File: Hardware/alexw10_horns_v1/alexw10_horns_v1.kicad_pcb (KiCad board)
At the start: 2 copper layers, 50 x 34 mm, 28 parts, among them J1 Conn_01x03, J2 Conn_01x02, J3 Conn_01x02, J4 Conn_01x02, Q1 Q_NMOS_DGS, SW1 SW_Push_SPDT

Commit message: finished horns
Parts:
- C8: footprint Capacitor_SMD:CP_Elec_8x5.4 -> Capacitor_SMD:CP_Elec_6.3x7.7
- D1: footprint Diode_SMD:D_1812_4532Metric -> Diode_SMD:D_1206_3216Metric
- moved D1 0.86 mm to (131.5, 81.0)
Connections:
- SW1 pad 1: /V_divider3.3V -> /HORN_CTL
- SW1 pad 3: /HORN_CTL -> /V_divider3.3V
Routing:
- net /V_divider3.3V: track 15.0 -> 18.3 mm, vias 0 -> 2
- net /HORN_CTL: track 14.0 -> 16.3 mm
- net /HORN_IN: track 21.9 -> 22.6 mm

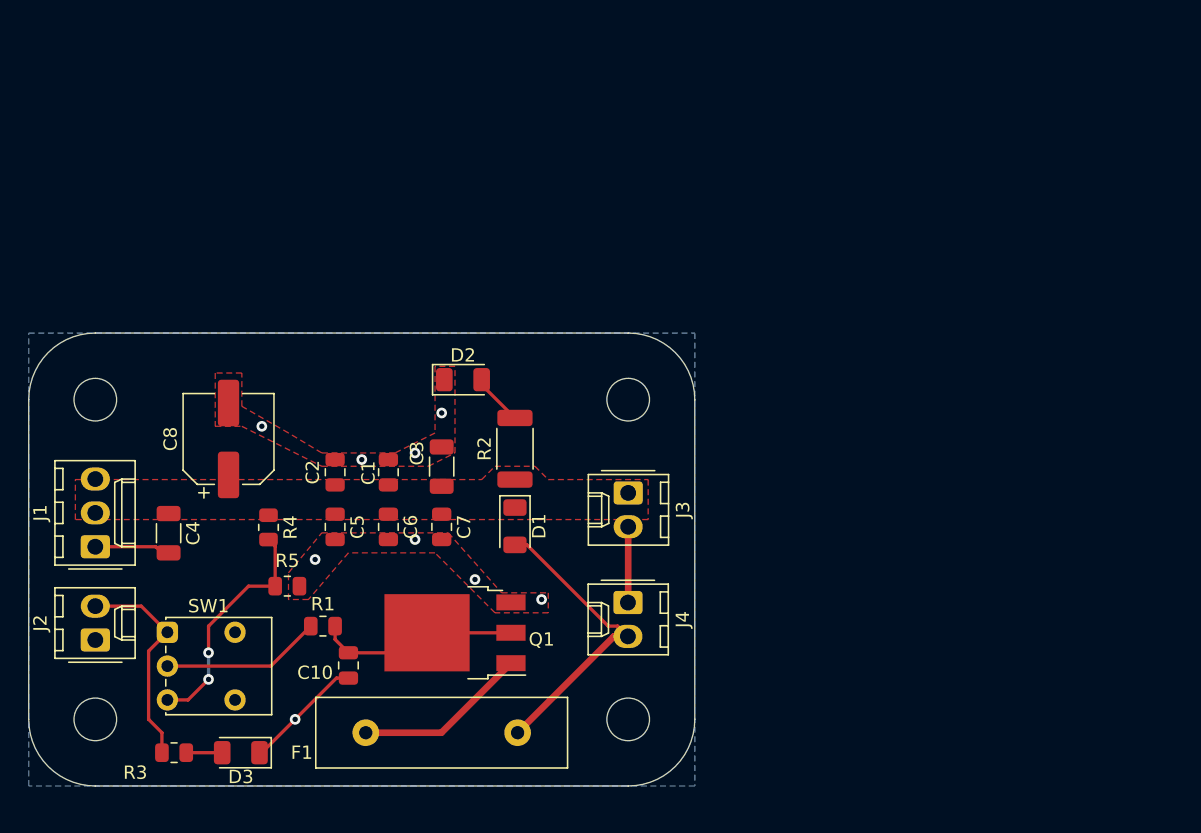
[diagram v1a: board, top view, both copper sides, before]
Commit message: fixed things related to horns such as changing connectors, removing the switch, and removing power planes as well as general rerouting of everything
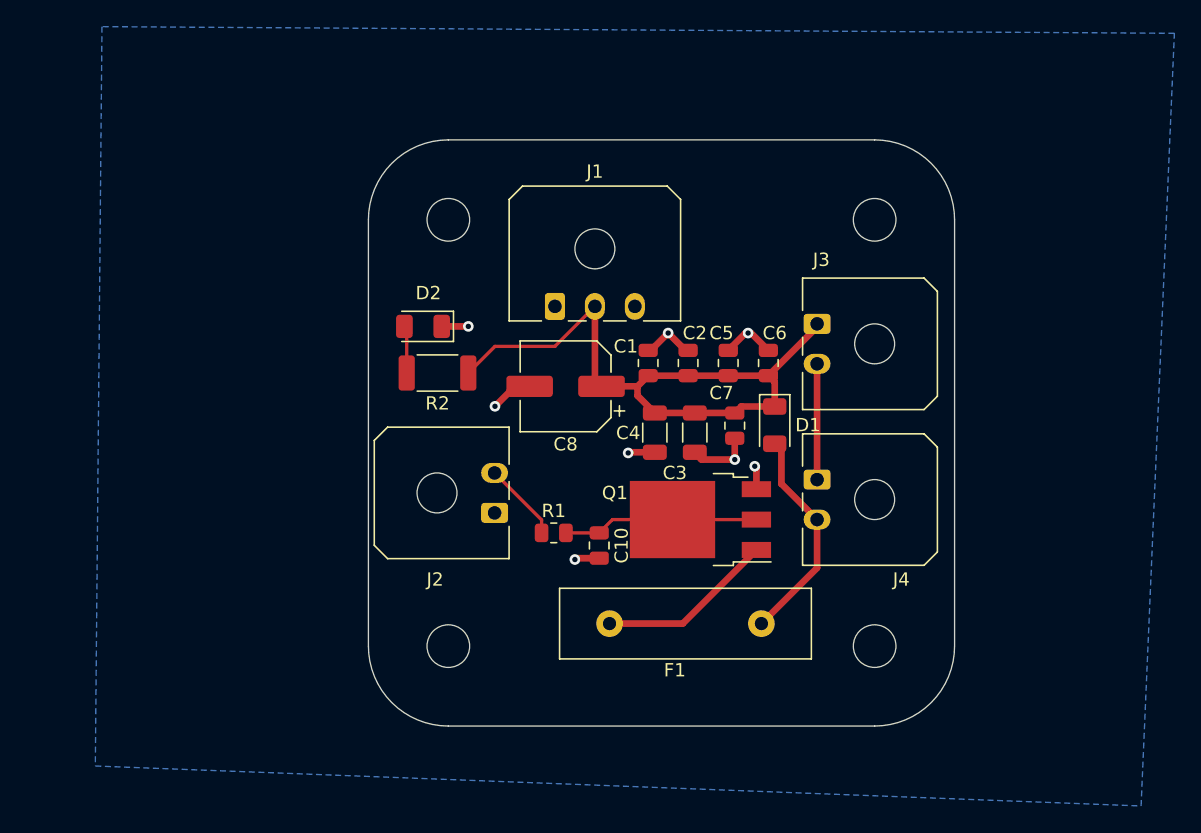
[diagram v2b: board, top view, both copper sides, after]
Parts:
- removed D3: GREEN_LED, LED_SMD:LED_1206_3216Metric
- removed R3: 130, Resistor_SMD:R_0805_2012Metric
- removed R4: 15k, Resistor_SMD:R_0805_2012Metric
- removed R5: 2.4k, Resistor_SMD:R_0805_2012Metric
- removed the REF** at (100.0, 71.5)
- removed the REF** at (100.0, 95.5)
- removed the REF** at (140.0, 71.5)
- removed the REF** at (140.0, 95.5)
- removed SW1: SW_Push_SPDT, Button_Switch_THT:SW_Push_1P2T_Vertical_E-Switch_800UDP8P1A1M6
- added REF**: MountingHole_3.2mm_M3, MountingHole:MountingHole_3.2mm_M3, F.Cu at (158.5, 58.0)
- added REF**: MountingHole_3.2mm_M3, MountingHole:MountingHole_3.2mm_M3, F.Cu at (158.5, 90.0)
- added REF**: MountingHole_3.2mm_M3, MountingHole:MountingHole_3.2mm_M3, F.Cu at (126.5, 58.0)
- added REF**: MountingHole_3.2mm_M3, MountingHole:MountingHole_3.2mm_M3, F.Cu at (126.5, 90.0)
- J1: footprint Connector_Molex:Molex_KK-254_AE-6410-03A_1x03_P2.54mm_Vertical -> Connector_Molex:Molex_Micro-Fit_3.0_43650-0300_1x03_P3.00mm_Horizontal
- J2, J3, J4: footprint Connector_Molex:Molex_KK-254_AE-6410-02A_1x02_P2.54mm_Vertical -> Connector_Molex:Molex_Micro-Fit_3.0_43650-0200_1x02_P3.00mm_Horizontal
- moved J1 38.9 mm to (134.5, 64.5), turned to 0 degrees
- moved C4 37.3 mm to (142.0, 74.0)
- moved C5 32.0 mm to (147.5, 68.8), turned to 90 degrees
- moved J2 31.5 mm to (130.0, 80.0)
- moved C6 31.1 mm to (150.5, 68.8), turned to 90 degrees
- moved C2 27.7 mm to (144.5, 68.8)
- moved C8 25.6 mm to (135.3, 70.5), turned to 180 degrees
- moved C7 23.3 mm to (148.0, 73.5)
- moved C1 21.2 mm to (141.5, 68.8)
- moved D1 20.9 mm to (151.0, 73.4)
- moved C10 20.9 mm to (137.8, 82.5)
- moved Q1 20.3 mm to (145.4, 80.5)
- moved F1 20.0 mm to (150.0, 88.3)
- moved C3 19.2 mm to (145.0, 74.0), turned to -90 degrees
- moved J3 19.0 mm to (154.2, 65.8)
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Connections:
- net Net-(D2-A) renamed /led
- R1 pad 1: /SW_OUT -> /HORN_CTL
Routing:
- net +24V: track 0.00 -> 50.3 mm
- net /V_divider3.3V: track 18.3 -> 0.00 mm, vias 2 -> 0
- net /SW_OUT: track 12.0 -> 0.00 mm
- net /HORN_CTL: track 16.3 -> 5.96 mm
- net GND: track 14.7 -> 23.9 mm, vias 9 -> 8
- net /HORN_IN: track 22.6 -> 16.5 mm
- net /HORN_CTL_filtered: track 18.8 -> 14.7 mm
- net /HORN_MIDDLE: track 5.70 -> 8.69 mm
- net Net-(D3-A): track 2.70 -> 0.00 mm
- removed copper zone on F.Cu, net +24V
- removed copper zone on F.Cu, net GND
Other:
- board size 50 x 34 mm -> 44 x 44 mm
